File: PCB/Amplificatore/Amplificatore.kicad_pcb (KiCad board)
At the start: 2 copper layers, 200 x 70 mm, 107 parts, among them J1 POT-GAIN, J10 PWR_VALVE1, J11 LOCAL_SWITCHES, J12 REMOTE_SWITCHES, J13 LED_SWITCHES, J14 POWER-STAGE, J15 LINE-OUT, J16 Conn_01x01, J17 Conn_01x01, J18 Conn_01x01, J19 Conn_01x01, J2 POT-LEAD, J20 PWR_DC, J21 PWR_VALVE2, J3 SEND-RETURN, J4 In, J5 POT-BASS-BACK, J6 POT-MID, J7 POT-TREBLE, J8 POT-BASS-FRONT, J9 MASTER, K1 G5Q-1, K2 G5Q-1, K3 G5Q-1, K4 G5Q-1, U1 ECC83, U2 ECC83, U3 TL082, U4 TL082

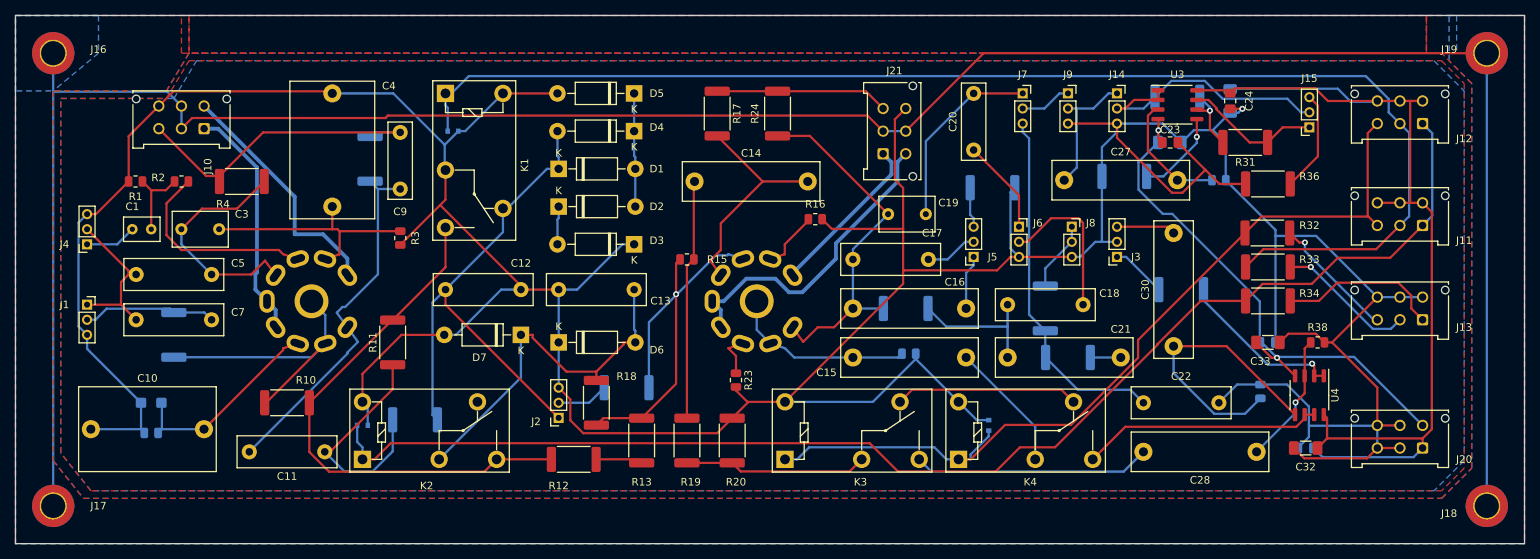
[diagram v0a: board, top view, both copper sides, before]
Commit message: Ultima release rimasterizzata per aumentare le distanze. Questa è stataprodotta da JLCPCB
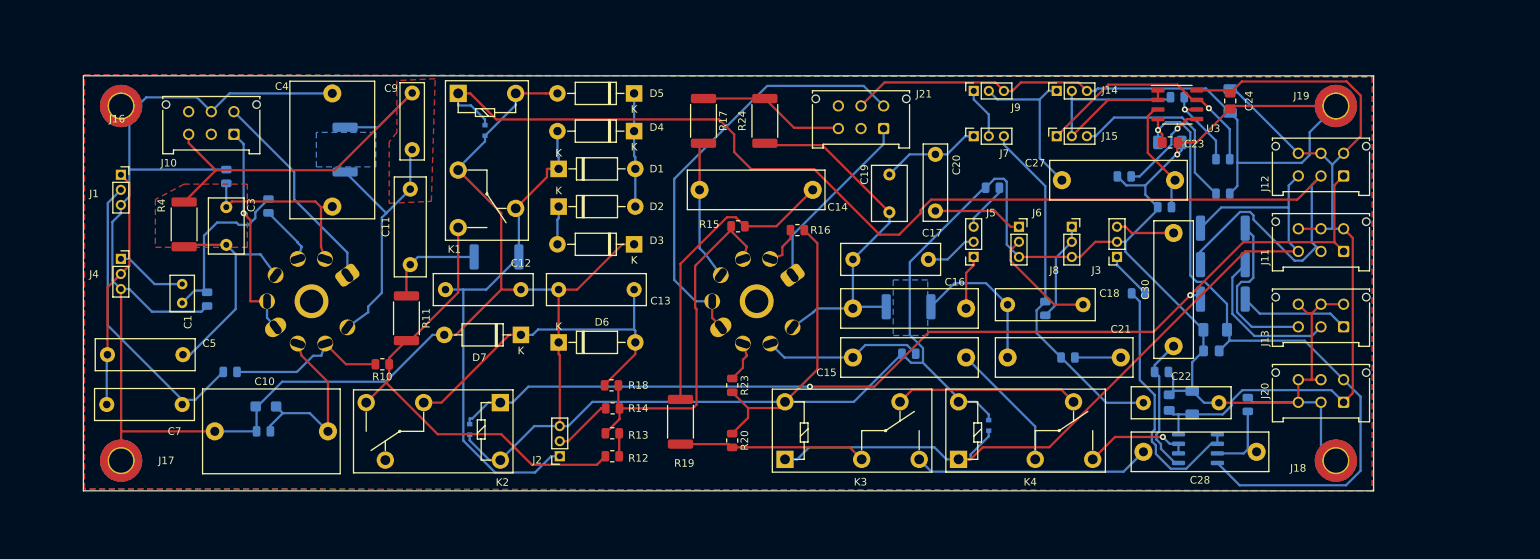
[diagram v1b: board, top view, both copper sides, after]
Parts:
- C32, C33, R1, R2, R3, R32, R33, R34, R38, U4: moved to B.Cu
- R10, R12, R13, R18, R20, R21, R25, R27, R28, R29, R30, R6: footprint Resistor_SMD:R_2512_6332Metric -> Resistor_SMD:R_0805_2012Metric
- R14: footprint Resistor_SMD:R_2512_6332Metric -> Resistor_SMD:R_0805_2012Metric; moved to F.Cu
- R31, R36: footprint Resistor_SMD:R_2512_6332Metric -> Resistor_SMD:R_0805_2012Metric; moved to B.Cu
- U1, U2: footprint Valve:Valve_ECC-83-2 -> Valve:Valve_ECC-83-3
- moved J15 33.5 mm to (178.0, 46.0), turned to 90 degrees
- moved C11 27.3 mm to (92.3, 63.0), turned to 90 degrees
- moved R3 24.5 mm to (67.9, 51.3), turned to 90 degrees
- moved R9 24.1 mm to (103.8, 62.0)
- moved J19 21.2 mm to (215.0, 42.0)
- moved J18 20.9 mm to (215.0, 89.0)
- moved K2 19.8 mm to (104.3, 81.3), turned to 180 degrees
- moved C31 19.1 mm to (192.9, 81.3), turned to 90 degrees
- moved R1 18.3 mm to (65.4, 67.6), turned to 90 degrees
- moved J1 17.8 mm to (54.0, 51.1)
- moved C10 16.4 mm to (66.4, 85.1)
- moved U4 16.4 mm to (196.7, 87.4), turned to 180 degrees
- moved C32 16.2 mm to (196.0, 81.3), turned to 90 degrees
- moved C14 15.7 mm to (145.7, 53.1), turned to 180 degrees
- moved C8 15.2 mm to (73.2, 81.8)
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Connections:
- J10 pad 2: Earth -> (no net)
- J10 pad 5: Earth -> GND
- J10 pad 6: GND -> (no net)
- J16 pad 1: Earth -> GND
- J17 pad 1: Earth -> GND
- J18 pad 1: Earth -> GND
- J19 pad 1: Earth -> GND
- J21 pad 2: Earth -> (no net)
- J21 pad 5: Earth -> GND
- J21 pad 6: GND -> (no net)
- R1 pad 1: Net-(C1-Pad1) -> GND
- R1 pad 2: GND -> Net-(C1-Pad1)
- R13 pad 1: Net-(R13-Pad1) -> Net-(R12-Pad1)
- R13 pad 2: Net-(R12-Pad1) -> Net-(R13-Pad2)
- R14 pad 1: Net-(R13-Pad1) -> Net-(J2-Pad2)
- R14 pad 2: Net-(J2-Pad2) -> Net-(R13-Pad2)
- R15 pad 1: Net-(R13-Pad1) -> Net-(C14-Pad1)
- R15 pad 2: Net-(C14-Pad1) -> Net-(R13-Pad2)
- R18 pad 1: Net-(R13-Pad1) -> Net-(R13-Pad2)
- R21 pad 1: Net-(R21-Pad1) -> Net-(J3-Pad1)
- R21 pad 2: Net-(J3-Pad1) -> Net-(R21-Pad2)
- R22 pad 1: /FILTRO_IN -> GND
- R22 pad 2: GND -> /FILTRO_IN
- R25 pad 1: Net-(J5-Pad3) -> GND
- R25 pad 2: GND -> Net-(J5-Pad3)
- R28 pad 1: Net-(C22-Pad2) -> Net-(J8-Pad1)
- R28 pad 2: Net-(J8-Pad1) -> Net-(C22-Pad2)
- R35 pad 1: Net-(C27-Pad2) -> GND
- R35 pad 2: GND -> Net-(C27-Pad2)
- R36 pad 1: GND -> Net-(J15-Pad3)
- R36 pad 2: Net-(J15-Pad3) -> GND
- R6 pad 1: Net-(R10-Pad2) -> Net-(C7-Pad1)
- R6 pad 2: Net-(C7-Pad1) -> Net-(R10-Pad2)
- U2 pad 7: Net-(R13-Pad1) -> Net-(R13-Pad2)
- U4 pad 1: Net-(R21-Pad1) -> Net-(R21-Pad2)
- U4 pad 2: Net-(R21-Pad1) -> Net-(R21-Pad2)
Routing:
- net Earth: track 319.6 -> 0.00 mm
- net Net-(R13-Pad1): track 54.6 -> 0.00 mm, vias 1 -> 0
- net Net-(R13-Pad2): track 0.00 -> 48.0 mm
- net GND: track 590.2 -> 630.3 mm
- net /RITHM-SW: track 175.8 -> 137.6 mm, vias 0 -> 2
- net Net-(R21-Pad2): track 0.00 -> 34.5 mm
- net Net-(C7-Pad1): track 17.7 -> 40.2 mm
- net Net-(R21-Pad1): track 22.4 -> 0.00 mm, vias 1 -> 0
- net /VEE: track 73.1 -> 93.8 mm, vias 2 -> 1
- net Net-(C30-Pad1): track 38.0 -> 18.4 mm
- net /VDD: track 137.6 -> 118.5 mm
- net Net-(R2-Pad2): track 26.9 -> 8.02 mm
- net Net-(K4-Pad3): track 32.1 -> 14.3 mm, vias 0 -> 1
- net Net-(C11-Pad1): track 31.0 -> 13.2 mm
- net Net-(R10-Pad2): track 38.5 -> 21.5 mm
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- removed copper zone on B.Cu, net Earth
- removed copper zone on F.Cu, net Earth
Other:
- board size 200 x 70 mm -> 171 x 55 mm
- net class FILAMENTO: clearance 0.5 -> 1; trace_width 0.5 -> 0.3
- net class HV: clearance 1 -> 2
